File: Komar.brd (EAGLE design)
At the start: 59.2 x 59.2 mm, 113 parts, among them CON1 USB-VERTICAL, CON10 PINHEAD_1X01-2, CON11 PINHEAD_1X01-2, CON12 PINHEAD_1X01-2, CON13 PINHEAD_1X01-2, CON14 PINHEAD_1X01-2, CON15 PINHEAD_1X01-2, CON2 PINHEAD_1X01-2, CON3 CON-4P-TABS-STRAIGHT, CON4 CON-4P-TABS-STRAIGHT, CON5 CON-4P-TABS-STRAIGHT, CON6 CON-4P-TABS-STRAIGHT, CON7 CON-4P-TABS-STRAIGHT, CON8 PINHEAD_1X04-2, CON9 PINHEAD_1X01-2, IC1 TPD3S014DBVR-SOT23-6, IC2 TPD3S014DBVR-SOT23-6, IC3 ATA6561-GBQW-N-HVSON8, IC4 ATA6561-GBQW-N-HVSON8, IC5 MCP9700AT-E/TTVAO-SOT23, IC6 11LC040T-E/TT, Q1 FDMS86368-F085, Q10 FDMS86368-F085, Q11 FDMS86368-F085, Q12 FDMS86368-F085, Q2 FDMS86368-F085, Q3 FDMS86368-F085, Q4 FDMS86368-F085, Q5 FDMS86368-F085, Q6 FDMS86368-F085, Q7 FDMS86368-F085, Q8 FDMS86368-F085, Q9 FDMS86368-F085

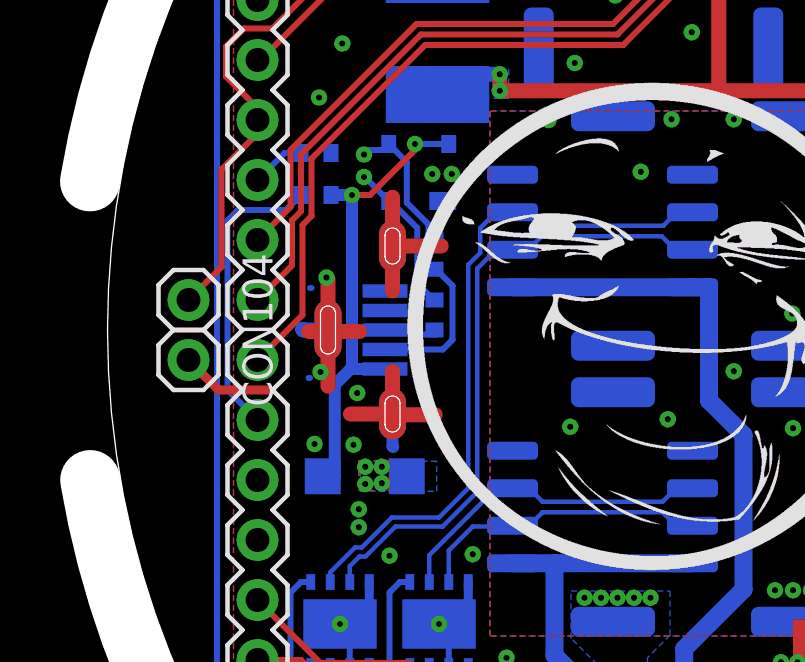
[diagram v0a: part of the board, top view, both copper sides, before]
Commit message: changed usb back to through-hole
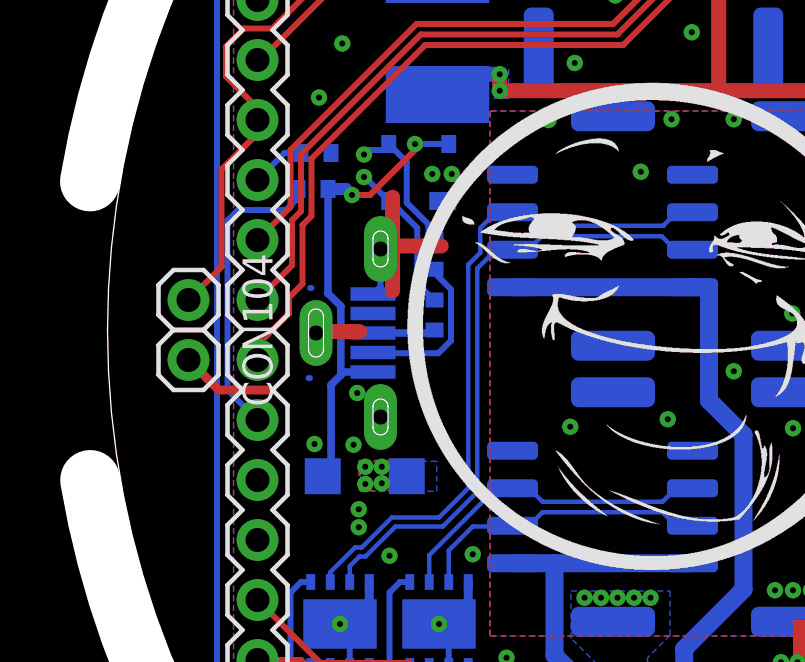
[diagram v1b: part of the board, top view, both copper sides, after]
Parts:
- removed CON1: USB-VERTICAL, Connectors:1051330011
- added J1: 105133-0011, 105133-0011:MOLEX_105133-0011
- moved R6 0.22 mm to (6.85, 33.7)
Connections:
- removed net N$52: CON1.3, R19.2
- removed net N$54: CON1.2, R20.2
- new net N$1: J1.3, R19.2
- new net N$2: J1.2, R20.2
- net GND: now also J1.5, J1.S1, J1.S2, J1.S3; no longer CON1.5, CON1.P$1, CON1.P$2, CON1.P$3, CON1.P$4, CON1.P$5, CON1.P$6
- net USB_VBUS: now also J1.1; no longer CON1.1
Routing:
- net GND: track 36.9 -> 21.3 mm, vias 45 -> 43
- net N$2: track 0.00 -> 5.39 mm
- net N$54: track 5.01 -> 0.00 mm
- net N$1: track 0.00 -> 2.19 mm
- net N$52: track 2.12 -> 0.00 mm

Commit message: minor changes to fixes #26
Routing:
- net GND: track 21.3 -> 20.4 mm
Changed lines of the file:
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@@
 <layer number="17" name="Pads" color="2" fill="1" visible="yes" active="yes"/>
 <layer number="18" name="Vias" color="2" fill="1" visible="yes" active="yes"/>
-<layer number="19" name="Unrouted" color="6" fill="1" visible="no" active="yes"/>
+<layer number="19" name="Unrouted" color="6" fill="1" visible="yes" active="yes"/>
 <layer number="20" name="Dimension" color="24" fill="1" visible="no" active="yes"/>
 <layer number="21" name="tPlace" color="7" fill="1" visible="no" active="yes"/>
@@
 <via x="8.15" y="16.1" extent="1-16" drill="0.2" diameter="0.55"/>
 <wire x1="2.7" y1="28" x2="3.7" y2="27" width="0.3" layer="1"/>
-<wire x1="3.7" y1="27" x2="5.4" y2="27" width="0.3" layer="1"/>
+<wire x1="3.7" y1="27" x2="4.5" y2="27" width="0.3" layer="1"/>
 <contactref element="CON8" pad="1"/>
 <via x="21.025" y="50.8" extent="1-16" drill="0.2" diameter="0.55"/>
@@
 <via x="10.25" y="35.2" extent="1-16" drill="0.2" diameter="0.55"/>
 <via x="8.15" y="33.5" extent="1-16" drill="0.2" diameter="0.55"/>
-<wire x1="7.175" y1="24.125" x2="7.4" y2="24.125" width="0.4" layer="16"/>
+<wire x1="7.4" y1="24.125" x2="7.175" y2="24.125" width="0.4" layer="16"/>
 <contactref element="R6" pad="2"/>
-<wire x1="7.4" y1="24.125" x2="7.575" y2="24.125" width="0.4" layer="16"/>
 <wire x1="8.15" y1="33.5" x2="7.95" y2="33.7" width="0.4" layer="16"/>
 <wire x1="7.95" y1="33.7" x2="7.35" y2="33.7" width="0.4" layer="16"/>
@@
 <wire x1="7.35" y1="33.7" x2="7.35" y2="30.21955625" width="0.254" layer="16"/>
 <wire x1="7.35" y1="30.21955625" x2="7.777" y2="29.79255625" width="0.254" layer="16"/>
-<wire x1="7.777" y1="29.79255625" x2="7.777" y2="27.5" width="0.254" layer="16"/>
-<wire x1="7.777" y1="27.5" x2="7.777" y2="27.49635" width="0.254" layer="16"/>
-<wire x1="7.777" y1="27.49635" x2="7.452" y2="27.17135" width="0.254" layer="16"/>
-<wire x1="7.452" y1="27.17135" x2="7.452" y2="24.177" width="0.254" layer="16"/>
-<wire x1="7.452" y1="24.177" x2="7.4" y2="24.125" width="0.254" layer="16"/>
+<wire x1="7.777" y1="29.79255625" x2="7.777" y2="27.7" width="0.254" layer="16"/>
+<wire x1="7.777" y1="27.7" x2="7.777" y2="27.5" width="0.254" layer="16"/>
+<wire x1="7.777" y1="27.49635" x2="7.777" y2="27.5" width="0.254" layer="16"/>
 <wire x1="8.85" y1="27.6" x2="7.877" y2="27.6" width="0.254" layer="16"/>
 <wire x1="7.877" y1="27.6" x2="7.777" y2="27.5" width="0.254" layer="16"/>
+<wire x1="7.777" y1="27.5" x2="7.777" y2="27.13265" width="0.254" layer="16"/>
+<wire x1="7.648" y1="24.373" x2="7.4" y2="24.125" width="0.254" layer="16"/>
+<wire x1="7.777" y1="27.13265" x2="7.648" y2="27.00365" width="0.254" layer="16"/>
+<wire x1="7.648" y1="27.00365" x2="7.648" y2="24.373" width="0.254" layer="16"/>
 </signal>
 <signal name="N$55">
@@
 <contactref element="R19" pad="2"/>
 <contactref element="J1" pad="3"/>
-<wire x1="8.85" y1="28.8" x2="8.85" y2="28.9" width="0.2" layer="16"/>
-<wire x1="9.1" y1="28.9" x2="10.8" y2="28.9" width="0.254" layer="16"/>
 <wire x1="10.8" y1="28.9" x2="10.9" y2="29" width="0.254" layer="16"/>
-<wire x1="8.85" y1="28.9" x2="9.1" y2="28.9" width="0.2" layer="16"/>
+<wire x1="8.85" y1="28.9" x2="10.8" y2="28.9" width="0.2" layer="16"/>
 </signal>
 <signal name="N$2">

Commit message: changes related to #26
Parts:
- moved D2 0.58 mm to (8.28, 23.6)
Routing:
- net VDD_5V: track 155.6 -> 169.4 mm
- removed copper zone on layer 1, net VDD_5V
- removed copper zone on layer 15, net VDD_5V

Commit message: updated power via connection
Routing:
- net VDD_5V: track 169.4 -> 158.7 mm
- added copper zone on layer 1, net VDD_5V
- added copper zone on layer 15, net VDD_5V
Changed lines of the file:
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@@
 <setting verticaltext="up"/>
 </settings>
-<grid distance="0.1" unitdist="mm" unit="mm" style="lines" multiple="29" display="yes" altdistance="0.1" altunitdist="mm" altunit="mm"/>
+<grid distance="0.01" unitdist="mm" unit="mm" style="lines" multiple="29" display="yes" altdistance="0.1" altunitdist="mm" altunit="mm"/>
 <layers>
 <layer number="1" name="Top" color="4" fill="1" visible="yes" active="yes"/>
@@
 <wire x1="11.375" y1="17.8" x2="11.375" y2="18.875" width="0.2" layer="16"/>
 <wire x1="11.375" y1="18.875" x2="11.075" y2="19.175" width="0.2" layer="16"/>
-<via x="9.3" y="21.275" extent="1-16" drill="0.2" diameter="0.55"/>
+<via x="9.12" y="21.195" extent="1-16" drill="0.2" diameter="0.55"/>
 <via x="12.175" y="21.525" extent="1-16" drill="0.2" diameter="0.55"/>
 <via x="29.375" y="43.85" extent="1-16" drill="0.2" diameter="0.55"/>
@@
 <contactref element="LED2" pad="A"/>
 <contactref element="R27" pad="2"/>
-<via x="8.09126875" y="24.04126875" extent="1-16" drill="0.2" diameter="0.55"/>
-<via x="8.84126875" y="23.44126875" extent="1-16" drill="0.2" diameter="0.55"/>
-<via x="8.69126875" y="24.06626875" extent="1-16" drill="0.2" diameter="0.55"/>
+<via x="8.69126875" y="23.93126875" extent="1-16" drill="0.2" diameter="0.55"/>
+<via x="8.08126875" y="23.32126875" extent="1-16" drill="0.2" diameter="0.55"/>
+<via x="8.09126875" y="23.93626875" extent="1-16" drill="0.2" diameter="0.55"/>
 <contactref element="D7" pad="2"/>
 <contactref element="D7" pad="5"/>
@@
 <wire x1="17.1" y1="46.975" x2="17.1" y2="46.475" width="0.4" layer="1"/>
 <contactref element="MODULE2" pad="40"/>
-<via x="8.24126875" y="23.49126875" extent="1-16" drill="0.2" diameter="0.55"/>
-<wire x1="11.725" y1="20.74163125" x2="8.801321875" y2="23.5014" width="0.5" layer="15"/>
-<wire x1="8.801321875" y1="23.5014" x2="8.44126875" y2="23.84126875" width="0.5" layer="15"/>
+<via x="8.69126875" y="23.31126875" extent="1-16" drill="0.2" diameter="0.55"/>
 <wire x1="11.725" y1="18.45" x2="14.025" y2="16.15" width="0.5" layer="15"/>
 <wire x1="14.025" y1="16.15" x2="20.075" y2="16.15" width="0.5" layer="15"/>
 <wire x1="21.5" y1="15" x2="21.225" y2="15" width="0.5" layer="15"/>
 <wire x1="21.225" y1="15" x2="20.075" y2="16.15" width="0.5" layer="15"/>
-<wire x1="11.725" y1="20.74163125" x2="11.725" y2="18.45" width="0.5" layer="15"/>
+<wire x1="11.725" y1="18.45" x2="11.725" y2="20.74163125" width="0.5" layer="15"/>
 <contactref element="IC6" pad="2"/>
 <contactref element="C15" pad="2"/>
@@
 <wire x1="20.7" y1="13.05" x2="20.75" y2="13" width="0.5" layer="1"/>
 <wire x1="18" y1="12.05" x2="18.55" y2="12.05" width="0.5" layer="1"/>
-<wire x1="8.69126875" y1="24" x2="8.69126875" y2="23.611453125" width="0.2" layer="15"/>
-<wire x1="8.69126875" y1="23.611453125" x2="8.801321875" y2="23.5014" width="0.2" layer="15"/>
-<wire x1="8.84126875" y1="23.44126875" x2="8.69126875" y2="23.59126875" width="0.508" layer="15"/>
-<wire x1="8.69126875" y1="23.59126875" x2="8.69126875" y2="23.94126875" width="0.508" layer="15"/>
-<wire x1="8.24126875" y1="23.49126875" x2="8.791190625" y2="23.49126875" width="0.508" layer="15"/>
-<wire x1="8.791190625" y1="23.49126875" x2="8.801321875" y2="23.5014" width="0.508" layer="15"/>
-<wire x1="8.69126875" y1="24.06626875" x2="9.23373125" y2="24.06626875" width="0.508" layer="16"/>
-<wire x1="9.23373125" y1="24.06626875" x2="9.6" y2="23.7" width="0.508" layer="16"/>
-<wire x1="9.6" y1="23.7" x2="9.675" y2="23.625" width="0.508" layer="16"/>
-<wire x1="8.84126875" y1="23.44126875" x2="9.34126875" y2="23.44126875" width="0.508" layer="16"/>
-<wire x1="9.34126875" y1="23.44126875" x2="9.6" y2="23.7" width="0.508" layer="16"/>
-<wire x1="8.84126875" y1="23.44126875" x2="8.84126875" y2="23.91626875" width="0.508" layer="16"/>
-<wire x1="8.71626875" y1="24.04126875" x2="8.69126875" y2="24.06626875" width="0.508" layer="16"/>
-<wire x1="8.09126875" y1="24.04126875" x2="8.71626875" y2="24.04126875" width="0.508" layer="16"/>
-<wire x1="8.71626875" y1="24.04126875" x2="8.84126875" y2="23.91626875" width="0.508" layer="16"/>
-<wire x1="8.24126875" y1="23.49126875" x2="8.69126875" y2="23.94126875" width="0.508" layer="15"/>
-<wire x1="8.69126875" y1="23.94126875" x2="8.69126875" y2="24" width="0.508" layer="15"/>
-<wire x1="8.84126875" y1="23.44126875" x2="8.79126875" y2="23.49126875" width="0.3048" layer="1"/>
-<wire x1="8.69126875" y1="23.59126875" x2="8.79126875" y2="23.49126875" width="0.3048" layer="1"/>
-<wire x1="8.24126875" y1="23.49126875" x2="8.09126875" y2="23.64126875" width="0.3048" layer="1"/>
-<wire x1="8.09126875" y1="23.64126875" x2="8.09126875" y2="23.7" width="0.3048" layer="1"/>
-<wire x1="8.09126875" y1="23.7" x2="8.09126875" y2="24.04126875" width="0.3048" layer="1"/>
-<wire x1="8.24126875" y1="23.49126875" x2="8.79126875" y2="23.49126875" width="0.3048" layer="1"/>
-<wire x1="8.09126875" y1="24.04126875" x2="8.11626875" y2="24.06626875" width="0.3048" layer="1"/>
-<wire x1="8.11626875" y1="24.06626875" x2="8.69126875" y2="24.06626875" width="0.3048" layer="1"/>
-<wire x1="8.69126875" y1="24.06626875" x2="8.69126875" y2="23.9" width="0.3048" layer="1"/>
-<wire x1="8.69126875" y1="23.9" x2="8.69126875" y2="23.59126875" width="0.3048" layer="1"/>
-<wire x1="8.69126875" y1="24.06626875" x2="8.09126875" y2="23.7" width="0.2" layer="1"/>
-<wire x1="8.24126875" y1="23.49126875" x2="8.69126875" y2="23.9" width="0.2" layer="1"/>
-<wire x1="8.69126875" y1="24.06626875" x2="8.24126875" y2="23.49126875" width="0.2" layer="1"/>
-<wire x1="8.69126875" y1="24.06626875" x2="8.09126875" y2="24.04126875" width="0.2" layer="15"/>
-<wire x1="8.29126875" y1="23.44126875" x2="8.4" y2="23.44126875" width="0.254" layer="16"/>
-<wire x1="8.4" y1="23.44126875" x2="8.84126875" y2="23.44126875" width="0.254" layer="16"/>
-<wire x1="8.16626875" y1="23.96626875" x2="8.09126875" y2="24.04126875" width="0.508" layer="16"/>
-<wire x1="8.24126875" y1="23.49126875" x2="8.16626875" y2="23.56626875" width="0.508" layer="16"/>
-<wire x1="8.16626875" y1="23.56626875" x2="8.16626875" y2="23.96626875" width="0.508" layer="16"/>
-<wire x1="8.24126875" y1="23.49126875" x2="8.29126875" y2="23.44126875" width="0.15" layer="16"/>
-<wire x1="8.69126875" y1="24.06626875" x2="8.4" y2="23.44126875" width="0.15" layer="16"/>
-<wire x1="8.84126875" y1="23.44126875" x2="8.16626875" y2="23.96626875" width="0.15" layer="16"/>
+<polygon width="0.1524" layer="15">
+<vertex x="7.81" y="23.31"/>
+<vertex x="7.81" y="24.04"/>
+<vertex x="7.94" y="24.17"/>
+<vertex x="8.84" y="24.17"/>
+<vertex x="8.95" y="24.06"/>
+<vertex x="8.95" y="23.17"/>
+<vertex x="8.84" y="23.06"/>
+<vertex x="7.9" y="23.06"/>
+<vertex x="7.81" y="23.15"/>
+<vertex x="7.81" y="23.27"/>
+<vertex x="7.81" y="23.28"/>
+<vertex x="7.8" y="23.29"/>
+</polygon>
+<wire x1="11.725" y1="20.74163125" x2="9.1553625" y2="23.31126875" width="0.508" layer="15"/>
+<wire x1="9.1553625" y1="23.31126875" x2="9.1453625" y2="23.32126875" width="0.508" layer="15"/>
+<wire x1="9.1453625" y1="23.32126875" x2="8.08126875" y2="23.32126875" width="0.508" layer="15"/>
+<polygon width="0.2" layer="1">
+<vertex x="7.9" y="24.16"/>
+<vertex x="7.82" y="24.08"/>
+<vertex x="7.82" y="23.1"/>
+<vertex x="7.9" y="23.02"/>
+<vertex x="8.08" y="23.02"/>
+<vertex x="8.91" y="23.02"/>
+<vertex x="8.97" y="23.08"/>
+<vertex x="8.97" y="24.14"/>
+<vertex x="8.93" y="24.18"/>
+<vertex x="7.95" y="24.18"/>
+<vertex x="7.93" y="24.18"/>
+</polygon>
+<wire x1="8.69126875" y1="23.31126875" x2="9.1553625" y2="23.31126875" width="0.508" layer="15"/>
+<polygon width="0.15" layer="16">
+<vertex x="7.89" y="24"/>
+<vertex x="7.89" y="23.21"/>
+<vertex x="7.93" y="23.17"/>
+<vertex x="8.03" y="23.07"/>
+<vertex x="8.04" y="23.07"/>
+<vertex x="10.25" y="23.07"/>
+<vertex x="10.27" y="23.09"/>
+<vertex x="10.27" y="24.15"/>
+<vertex x="10.2" y="24.22"/>
+<vertex x="8.01" y="24.22"/>
+<vertex x="7.91" y="24.12"/>
+<vertex x="7.89" y="24.1"/>
+<vertex x="7.89" y="24.02"/>
+</polygon>
+<wire x1="8.69126875" y1="23.93126875" x2="9.36873125" y2="23.93126875" width="0.508" layer="16"/>
+<wire x1="9.36873125" y1="23.93126875" x2="9.675" y2="23.625" width="0.508" layer="16"/>
+<wire x1="8.69126875" y1="23.31126875" x2="9.36126875" y2="23.31126875" width="0.508" layer="16"/>
+<wire x1="9.36126875" y1="23.31126875" x2="9.675" y2="23.625" width="0.508" layer="16"/>
 </signal>
 <signal name="CAN1_VDD">
